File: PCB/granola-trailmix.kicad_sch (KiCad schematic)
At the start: 46 parts, among them J1 Conn_01x02, J2 USB_B_Micro, SW1 6mm_Button, SW10 MX_Switch, SW11 MX_Switch, SW12 MX_Switch, SW13 MX_Switch, SW14 MX_Switch, SW15 MX_Switch, SW16 MX_Switch, SW17 MX_Switch, SW18 MX_Switch, SW2 6mm_Button, SW3 6mm_Button, SW4 6mm_Button, SW5 6mm_Button, SW6 6mm_Button, SW7 MX_Switch, SW8 MX_Switch, SW9 MX_Switch, U1 AMS1117-3.3_SOT223, U2 W25Q128JVS, U3 RP2040, Y1 ABLS-12.000MHZ-B4-T

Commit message: usb-c
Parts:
- removed J2: USB_B_Micro, Connector_USB:USB_Micro-B_Amphenol_10103594-0001LF_Horizontal, symbol RP2040_minimal-rescue:USB_B_Micro-Connector
- added R6, R7: 5.1k, Resistor_SMD:R_0402_1005Metric, symbol Device:R_Small
- added USB1: HRO-TYPE-C-31-M-12, Type-C:HRO-TYPE-C-31-M-12-Assembly, symbol Type-C:HRO-TYPE-C-31-M-12
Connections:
- net GND: now also R6.2, R7.2, USB1.1 (GND), USB1.12 (GND), USB1.13 (SHIELD)
- net USB_D+: now also USB1.6 (DP1), USB1.8 (DP2)
- net USB_D-: now also USB1.5 (DN2), USB1.7 (DN1)
- net VBUS: now also USB1.11 (VBUS), USB1.2 (VBUS)
- new net: R6.1, USB1.10 (CC2)
- new net: R7.1, USB1.4 (CC1)
- no-connect marks 16 -> 17
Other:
- note added: "Power / USB"
- note removed: "Power"
- moved on the sheet: C1, C10, C11, C12, C13, C14, C15, C16, C17, C2, C3, C4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

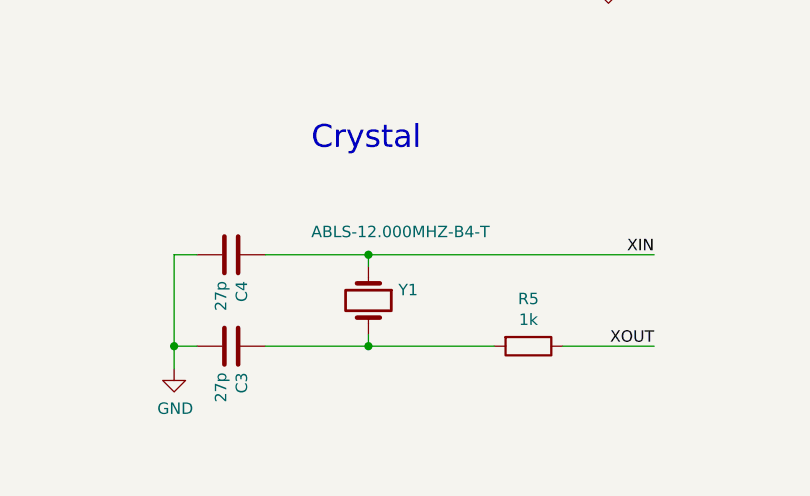
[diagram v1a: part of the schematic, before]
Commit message: Updated PCB to new crystal. Added version of TrailMix case that has no front design.
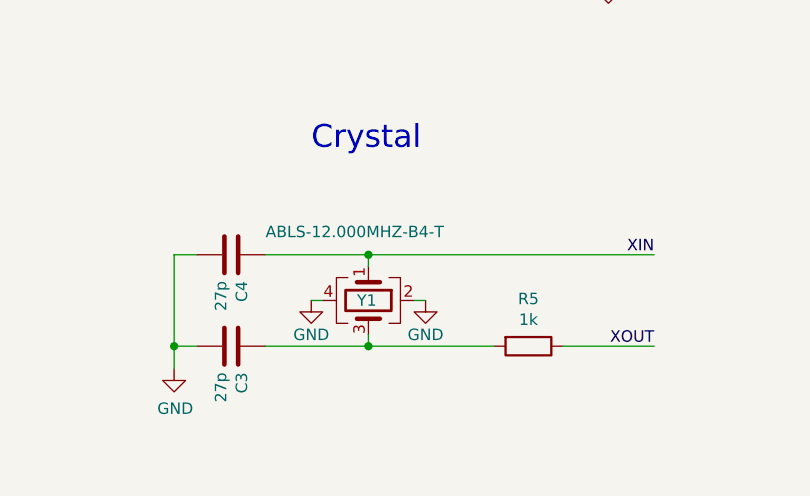
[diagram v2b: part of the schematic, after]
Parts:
- Y1: footprint RP2040_minimal:Crystal_SMD_HC49-US -> Crystal:Crystal_SMD_3225-4Pin_3.2x2.5mm; symbol Device:Crystal -> Device:Crystal_GND23; LCSC C390753 -> C9002
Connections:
- net GND: now also Y1.2, Y1.4
- net at C3.1, R5.2: now also Y1.3; no longer Y1.2
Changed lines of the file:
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@@
+    (stroke (width 0) (type default) (color 0 0 0 0))
+  )
+  (wire (pts (xy 72.39 203.2) (xy 71.12 203.2))
     (stroke (width 0) (type default) (color 0 0 0 0))
   )
@@
   )
   (wire (pts (xy 158.75 80.01) (xy 170.18 80.01))
+    (stroke (width 0) (type default) (color 0 0 0 0))
+  )
+  (wire (pts (xy 59.69 203.2) (xy 60.96 203.2))
     (stroke (width 0) (type default) (color 0 0 0 0))
   )
@@
     (pin "2")
   )
-  (symbol (lib_id "Device:Crystal") (at 66.04 203.2 270) (unit 1)
-    (in_bom yes) (on_board yes)
-    (property "Reference" "Y1" (id 0) (at 69.3674 202.0316 90)
-      (effects (font (size 1.27 1.27)) (justify left))
-    )
-    (property "Value" "ABLS-12.000MHZ-B4-T" (id 1) (at 59.69 195.58 90)
-      (effects (font (size 1.27 1.27)) (justify left))
-    )
-    (property "Footprint" "RP2040_minimal:Crystal_SMD_HC49-US" (id 2) (at 66.04 203.2 0)
+  (symbol (lib_id "Device:Crystal_GND23") (at 66.04 203.2 270) (unit 1)
+    (in_bom yes) (on_board yes)
+    (property "Reference" "Y1" (id 0) (at 64.77 203.2 90)
+      (effects (font (size 1.27 1.27)) (justify left))
+    )
+    (property "Value" "ABLS-12.000MHZ-B4-T" (id 1) (at 54.61 195.58 90)
+      (effects (font (size 1.27 1.27)) (justify left))
+    )
+    (property "Footprint" "Crystal:Crystal_SMD_3225-4Pin_3.2x2.5mm" (id 2) (at 66.04 203.2 0)
       (effects (font (size 1.27 1.27)) hide)
     )
@@
       (effects (font (size 1.27 1.27)) hide)
     )
-    (property "LCSC" "C390753" (id 4) (at 66.04 203.2 90)
-      (effects (font (size 1.27 1.27)) hide)
-    )
-    (pin "1")
-    (pin "2")
+    (property "LCSC" "C9002" (id 4) (at 66.04 203.2 90)
+      (effects (font (size 1.27 1.27)) hide)
+    )
+    (pin "1")
+    (pin "2")
+    (pin "3")
+    (pin "4")
   )
   (symbol (lib_id "MikesPCBLib:MX_Switch") (at 276.86 146.05 0) (unit 1)
@@
     (pin "1")
     (pin "2")
+  )
+  (symbol (lib_id "power:GND") (at 59.69 203.2 0) (unit 1)
+    (in_bom yes) (on_board yes)
+    (property "Reference" "#PWR0101" (id 0) (at 59.69 209.55 0)
+      (effects (font (size 1.27 1.27)) hide)
+    )
+    (property "Value" "GND" (id 1) (at 59.69 207.01 0))
+    (property "Footprint" "" (id 2) (at 59.69 203.2 0)
+      (effects (font (size 1.27 1.27)) hide)
+    )
+    (property "Datasheet" "" (id 3) (at 59.69 203.2 0)
+      (effects (font (size 1.27 1.27)) hide)
+    )
+    (pin "1")
   )
   (symbol (lib_id "Device:C") (at 236.22 85.09 0) (unit 1)
@@
     (pin "1")
   )
+  (symbol (lib_id "power:GND") (at 72.39 203.2 0) (unit 1)
+    (in_bom yes) (on_board yes)
+    (property "Reference" "#PWR0102" (id 0) (at 72.39 209.55 0)
+      (effects (font (size 1.27 1.27)) hide)
+    )
+    (property "Value" "GND" (id 1) (at 72.39 207.01 0))
+    (property "Footprint" "" (id 2) (at 72.39 203.2 0)
+      (effects (font (size 1.27 1.27)) hide)
+    )
+    (property "Datasheet" "" (id 3) (at 72.39 203.2 0)
+      (effects (font (size 1.27 1.27)) hide)
+    )
+    (pin "1")
+  )
   (symbol (lib_id "Device:C") (at 224.79 85.09 0) (unit 1)
     (in_bom yes) (on_board yes)
@@
       (reference "#PWR039") (unit 1) (value "GND") (footprint "")
     )
+    (path "/93f199ce-0eb1-431d-a0d5-82727b205bb8"
+      (reference "#PWR0101") (unit 1) (value "GND") (footprint "")
+    )
+    (path "/f4f7796f-84fd-4e2a-8fd6-473bbbc50669"
+      (reference "#PWR0102") (unit 1) (value "GND") (footprint "")
+    )
     (path "/a8017140-88d5-46c9-aca3-f312dae9784d"
       (reference "C1") (unit 1) (value "10u") (footprint "Capacitor_SMD:C_0805_2012Metric")
@@
     )
     (path "/258b39a7-cf44-4d3d-aa3c-e9aebbe1befb"
-      (reference "Y1") (unit 1) (value "ABLS-12.000MHZ-B4-T") (footprint "RP2040_minimal:Crystal_SMD_HC49-US")
-    )
-  )
+      (reference "Y1") (unit 1) (value "ABLS-12.000MHZ-B4-T") (footprint "Crystal:Crystal_SMD_3225-4Pin_3.2x2.5mm")
+    )
+  )
